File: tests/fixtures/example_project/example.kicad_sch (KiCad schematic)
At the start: 5 parts, among them J1 Conn_01x03_Pin, U1 LM321

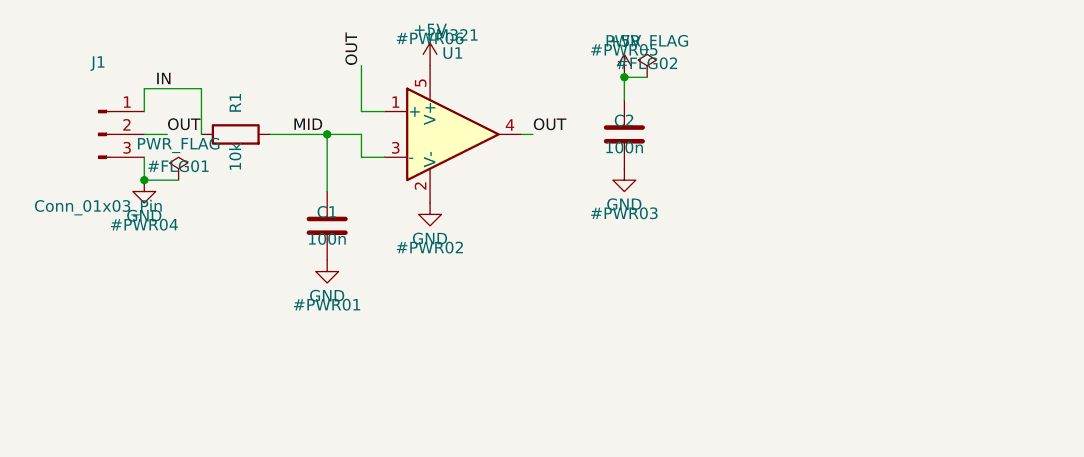
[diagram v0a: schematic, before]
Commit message: Gate the design instead of only reviewing it
A review answers "what is wrong with this design". That is the right
shape for a person, who reads the list and decides, and the wrong shape
for anything generating a design: it will emit a board, print a page of
warnings and move on, because nothing says which of those findings were
allowed to survive.

`eda gate` is that statement. It runs both reviews, applies a policy that
names which rules block and how many findings may remain, and exits 2
until the design meets it. A finding either blocks or appears under
`waived` next to the sentence somebody wrote to excuse it - a waiver with
no reason is refused - so excusing a violation is a diff a reviewer sees
rather than a step a generator can skip. Three policies ship: `default`
(what the reviews already enforce), `ai-generated` (everything a machine
can check has to be clean first) and `fabrication`.

The rules the gate needed did not exist, because ERC and DRC have no
opinion about any of them - a design can be clean under both and still be
one no engineer would sign:

* Drawing readability, none of which changes the netlist: geometry off
  the 1.27 mm grid (KiCad connects on exact coordinates, so this draws as
  a connection that is not one), a wire ending on another wire with no
  junction, dangling wire ends, overlapping symbols, items past the page
  border, diagonal wires, generated net names, sheet density, title block.
* Part specification, because a value is not a specification: missing
  voltage/tolerance/power ratings, capacitor derating against the rail it
  actually sits on, missing part numbers, and whether any sheet records
  why the design is the way it is.
* Artwork: silkscreen over pads and below the printer's limit, colliding
  pads, off-grid placement and odd rotations, decoupling with no via down
  to the plane, track stubs, acute corners, mixed track widths.

Both geometry families needed spatial indexing to stay usable: the
junction rule was quadrati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
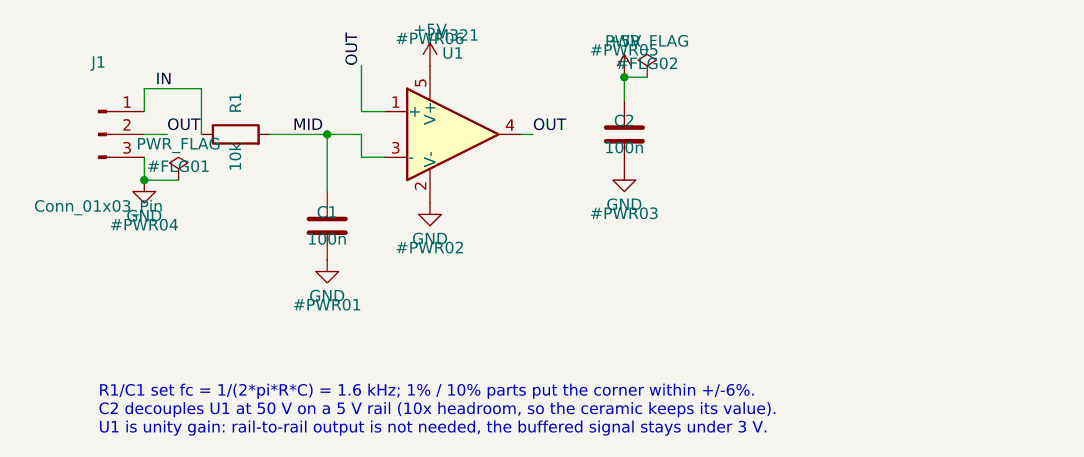
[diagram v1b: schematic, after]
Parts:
- C1, C2: Tolerance (none) -> 10%; Voltage (none) -> 50V
- J1: MPN (none) -> 61300311121; Manufacturer (none) -> Wurth Elektronik
- R1: Power (none) -> 0.125W; Tolerance (none) -> 1%
- U1: MPN (none) -> LM321MF/NOPB; Manufacturer (none) -> Texas Instruments
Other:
- note added: "R1/C1 set fc = 1/(2*pi*R*C) = 1.6 kHz; 1% / 10% parts put the corner within +/-6%. C2 decouples U1 at 50 V on a 5 V rail (10x headroom, so the ceramic keeps its value). U1 is unity gain: rail-to-rail output is not needed, the buffered signal stays under 3 V."
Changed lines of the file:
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@@
     (property "Footprint" "Connector_PinHeader_2.54mm:PinHeader_1x03_P2.54mm_Vertical" (at 88.9 60.96 0) (effects (font (size 1.27 1.27)) hide))
     (property "Datasheet" "~" (at 88.9 60.96 0) (effects (font (size 1.27 1.27)) hide))
+    (property "MPN" "61300311121" (at 88.9 60.96 0) (effects (font (size 1.27 1.27)) hide))
+    (property "Manufacturer" "Wurth Elektronik" (at 88.9 60.96 0) (effects (font (size 1.27 1.27)) hide))
     (pin "1")
     (pin "2")
@@
     (property "Footprint" "Resistor_SMD:R_0805_2012Metric" (at 104.14 60.96 0) (effects (font (size 1.27 1.27)) hide))
     (property "Datasheet" "~" (at 104.14 60.96 0) (effects (font (size 1.27 1.27)) hide))
+    (property "Tolerance" "1%" (at 104.14 60.96 0) (effects (font (size 1.27 1.27)) hide))
+    (property "Power" "0.125W" (at 104.14 60.96 0) (effects (font (size 1.27 1.27)) hide))
     (pin "1")
     (pin "2")
@@
     (property "Footprint" "Capacitor_SMD:C_0805_2012Metric" (at 114.3 71.12 0) (effects (font (size 1.27 1.27)) hide))
     (property "Datasheet" "~" (at 114.3 71.12 0) (effects (font (size 1.27 1.27)) hide))
+    (property "Voltage" "50V" (at 114.3 71.12 0) (effects (font (size 1.27 1.27)) hide))
+    (property "Tolerance" "10%" (at 114.3 71.12 0) (effects (font (size 1.27 1.27)) hide))
     (pin "1")
     (pin "2")
@@
     (property "Footprint" "Package_TO_SOT_SMD:SOT-23-5" (at 128.27 60.96 0) (effects (font (size 1.27 1.27)) hide))
     (property "Datasheet" "http://www.ti.com/lit/ds/symlink/lm321.pdf" (at 128.27 60.96 0) (effects (font (size 1.27 1.27)) hide))
+    (property "MPN" "LM321MF/NOPB" (at 128.27 60.96 0) (effects (font (size 1.27 1.27)) hide))
+    (property "Manufacturer" "Texas Instruments" (at 128.27 60.96 0) (effects (font (size 1.27 1.27)) hide))
     (pin "1")
     (pin "2")
@@
     (property "Footprint" "Capacitor_SMD:C_0805_2012Metric" (at 147.32 60.96 0) (effects (font (size 1.27 1.27)) hide))
     (property "Datasheet" "~" (at 147.32 60.96 0) (effects (font (size 1.27 1.27)) hide))
+    (property "Voltage" "50V" (at 147.32 60.96 0) (effects (font (size 1.27 1.27)) hide))
+    (property "Tolerance" "10%" (at 147.32 60.96 0) (effects (font (size 1.27 1.27)) hide))
     (pin "1")
     (pin "2")
@@
     (instances (project "example" (path "/00000000-0000-0000-0000-000000000001" (reference "#FLG02") (unit 1))))
   )
+  (text "R1/C1 set fc = 1/(2*pi*R*C) = 1.6 kHz; 1% / 10% parts put the corner within +/-6%.\nC2 decouples U1 at 50 V on a 5 V rail (10x headroom, so the ceramic keeps its value).\nU1 is unity gain: rail-to-rail output is not needed, the buffered signal stays under 3 V." (at 88.9 88.9 0) (effects (font (size 1.27 1.27)) (justify left top))
+)
   (sheet_instances
     (path "/" (page "1"))
